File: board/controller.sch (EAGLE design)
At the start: 70 parts, among them J1 X, J10 FEED_HOLD, J11 PROBE, J12 ERROR, J13 HOLDING, J14 GND, J15 MOTOR_CURRENT, J16 SD_READER, J17 WHEEL, J19 Z_DISPLAY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

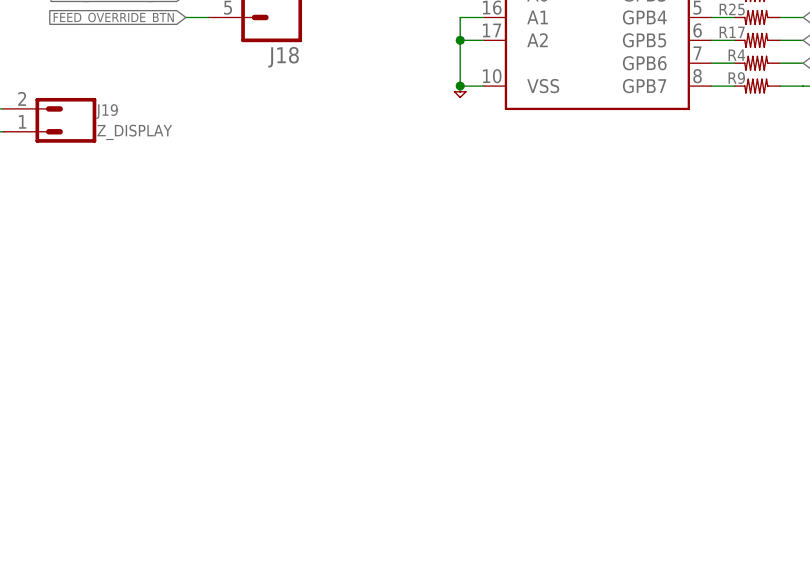
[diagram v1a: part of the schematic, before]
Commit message: updated wemos silk, added info to notes
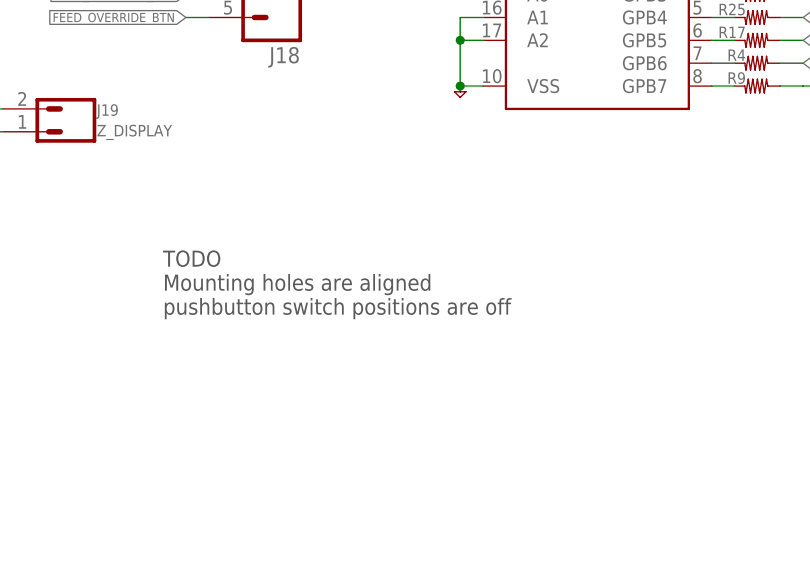
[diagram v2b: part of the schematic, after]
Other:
- note added: "TODO Mounting holes are aligned pushbutton switch positions are off"
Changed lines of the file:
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@@
 <text x="177.8" y="10.16" size="2.54" layer="97" align="top-left">180804</text>
 <text x="261.62" y="10.16" size="2.54" layer="97" align="top-left">v1.0</text>
+<text x="134.62" y="81.28" size="1.778" layer="97">TODO
+Mounting holes are aligned
+pushbutton switch positions are off</text>
 </plain>
 <instances>

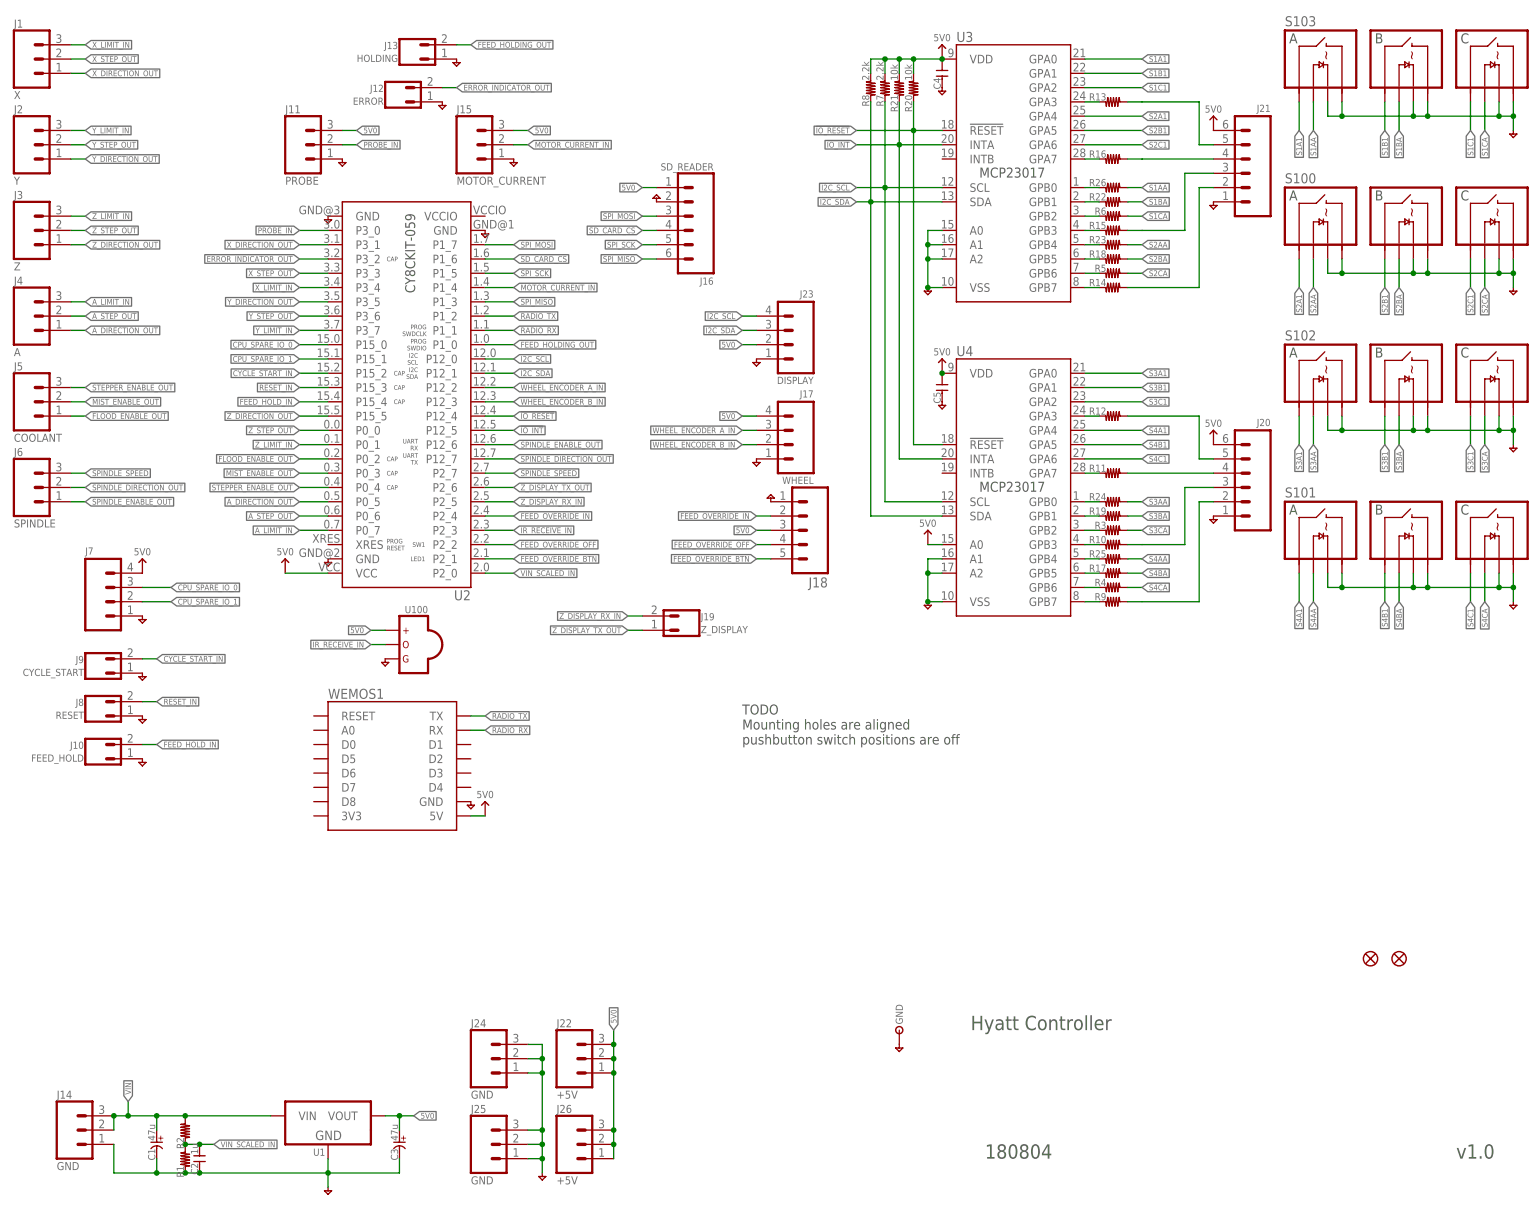
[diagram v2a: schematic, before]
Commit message: added component values to schematic cleaned up brd layout
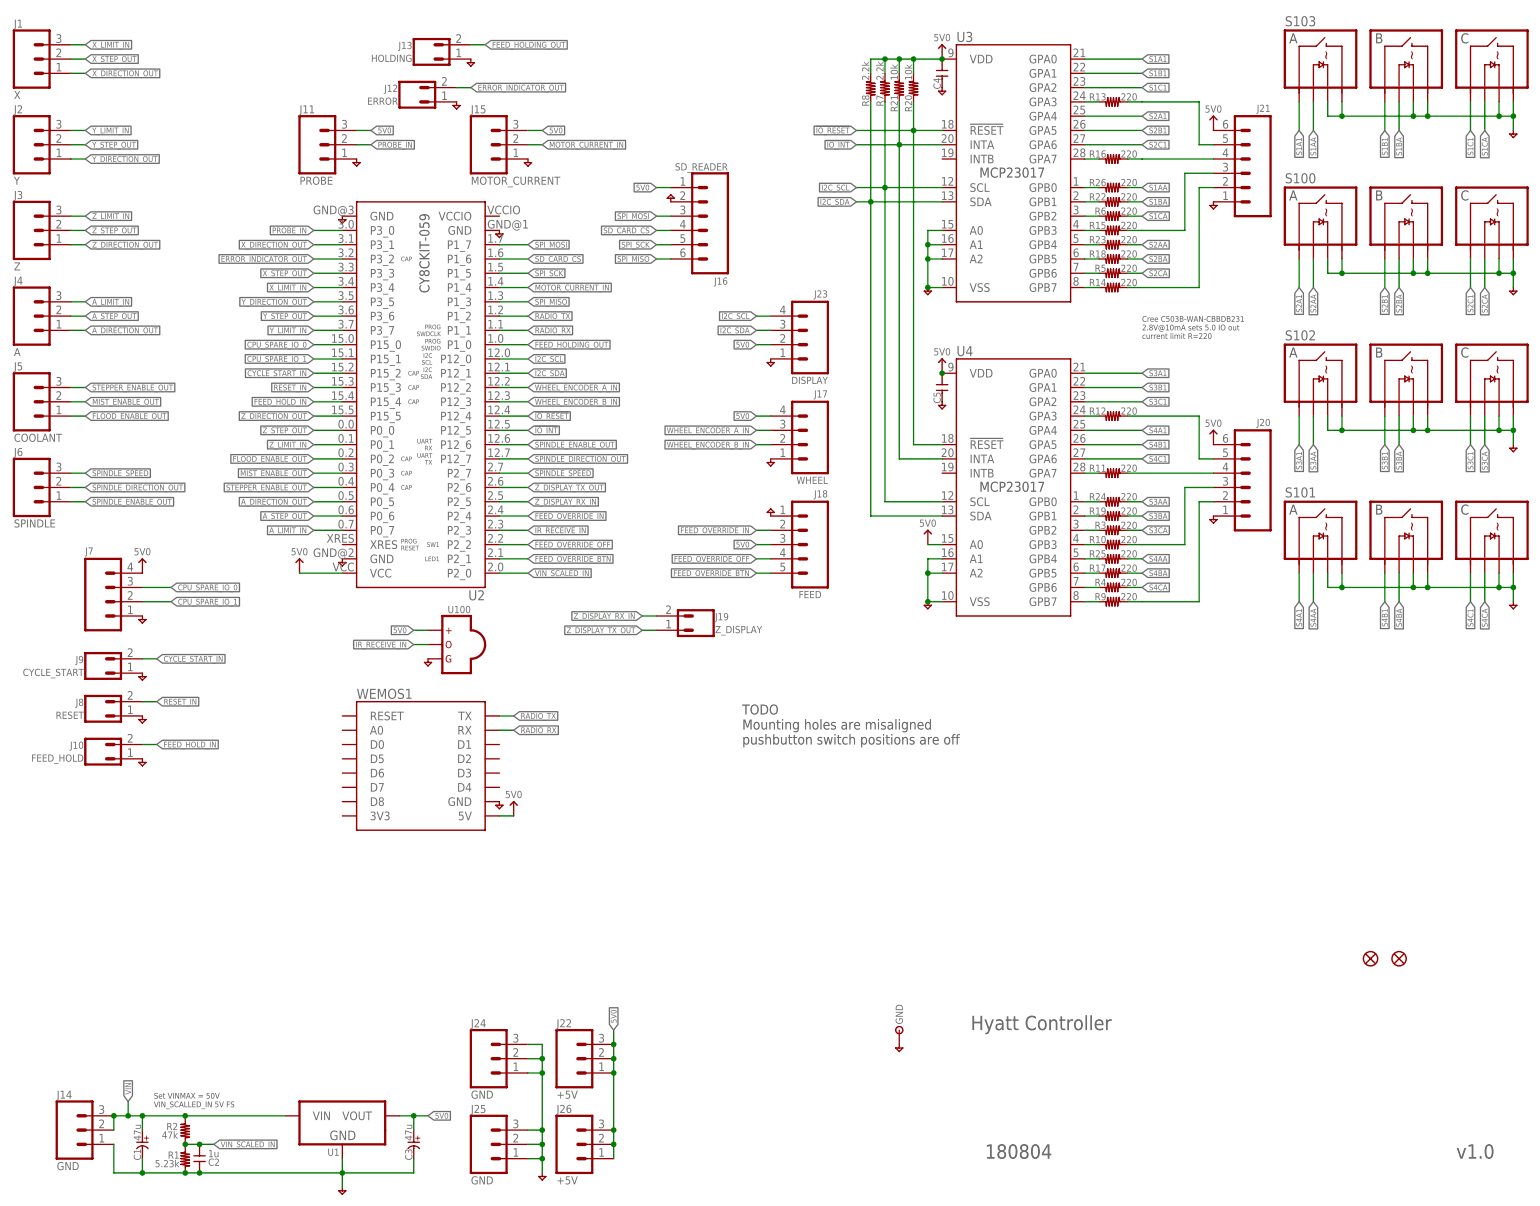
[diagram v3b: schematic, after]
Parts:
- J18: value (none) -> FEED
- R1: value (none) -> 5.23k
- R10, R11, R12, R13, R14, R15, R16, R17, R18, R19, R22, R23, R24, R25, R26, R3, R4, R5, R6, R9: value (none) -> 220
- R2: value (none) -> 47k
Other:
- note added: "Cree C503B-WAN-CBBDB231 2.8V@10mA sets 5.0 IO out current limit R=220"
- note added: "Set VINMAX = 50V VIN_SCALLED_IN 5V FS"
- note added: "TODO Mounting holes are misaligned pushbutton switch positions are off"
- note removed: "TODO Mounting holes are aligned pushbutton switch positions are off"
- moved on the sheet: C1, C3, J11, J12, J13, J15, J16, J17, J18, J19, J23, U1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

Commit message: updated schematic info initial add for rest
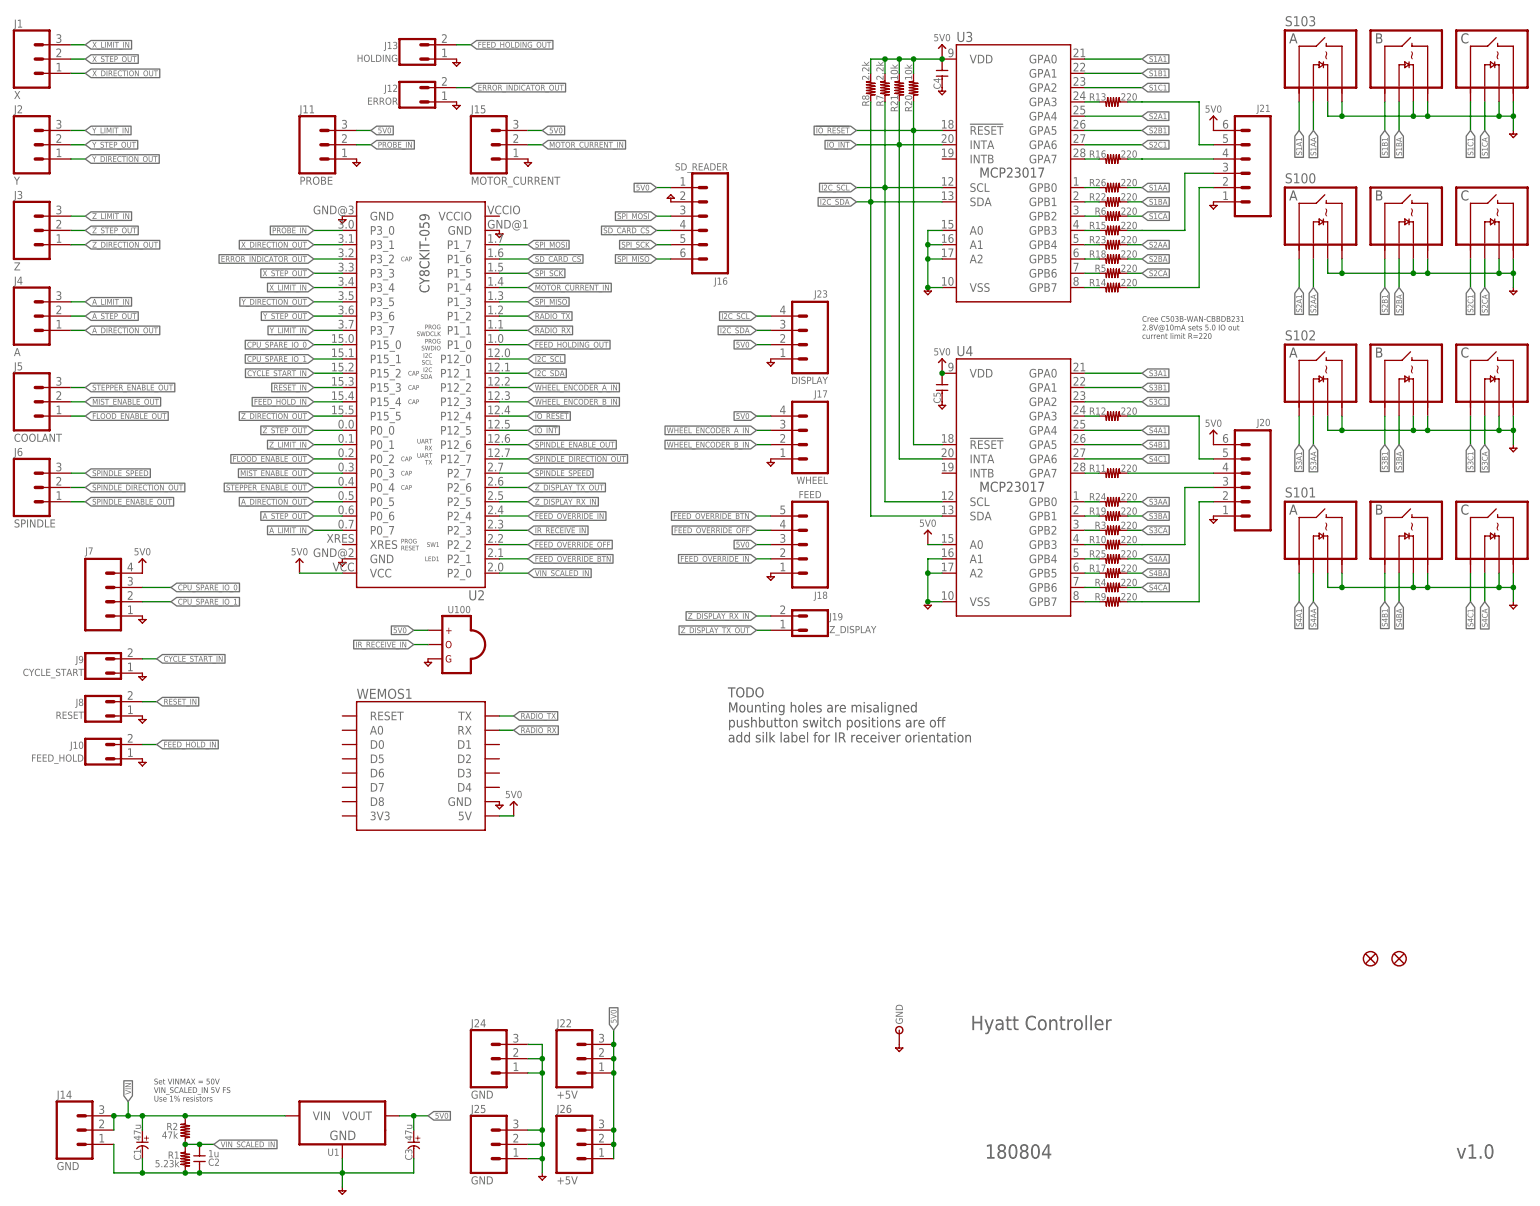
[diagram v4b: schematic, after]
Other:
- note added: "Set VINMAX = 50V VIN_SCALED_IN 5V FS Use 1% resistors"
- note added: "TODO Mounting holes are misaligned pushbutton switch positions are off add silk label for IR receiver orientation"
- note removed: "Set VINMAX = 50V VIN_SCALLED_IN 5V FS"
- note removed: "TODO Mounting holes are misaligned pushbutton switch positions are off"
- moved on the sheet: J13, J18, J19
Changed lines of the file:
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@@
 <text x="177.8" y="10.16" size="2.54" layer="97" align="top-left">180804</text>
 <text x="261.62" y="10.16" size="2.54" layer="97" align="top-left">v1.0</text>
-<text x="134.62" y="81.28" size="1.778" layer="97">TODO
+<text x="132.08" y="91.44" size="1.778" layer="97" align="top-left">TODO
 Mounting holes are misaligned
-pushbutton switch positions are off</text>
+pushbutton switch positions are off
+add silk label for IR receiver orientation</text>
 <text x="205.74" y="157.48" size="1.016" layer="97" align="top-left">Cree C503B-WAN-CBBDB231
 2.8V@10mA sets 5.0 IO out
 current limit R=220</text>
-<text x="29.972" y="19.304" size="1.016" layer="97" align="top-left">Set VINMAX = 50V
-VIN_SCALLED_IN 5V FS</text>
+<text x="29.972" y="21.844" size="1.016" layer="97" align="top-left">Set VINMAX = 50V
+VIN_SCALED_IN 5V FS
+Use 1% resistors</text>
 </plain>
 <instances>
@@
 <instance part="WEMOS1" gate="D1" x="76.2" y="76.2"/>
 <instance part="J8" gate="G$1" x="22.86" y="86.36"/>
-<instance part="J19" gate="G$1" x="124.46" y="101.6" rot="MR0"/>
+<instance part="J19" gate="G$1" x="144.78" y="101.6" rot="MR0"/>
 <instance part="J10" gate="G$1" x="22.86" y="78.74"/>
 <instance part="J9" gate="G$1" x="22.86" y="93.98"/>
@@
 <instance part="J11" gate="G$1" x="60.96" y="187.96"/>
 <instance part="GND12" gate="1" x="66.04" y="185.42"/>
-<instance part="GND13" gate="1" x="139.7" y="121.92" rot="R180"/>
+<instance part="GND13" gate="1" x="139.7" y="111.76" rot="MR0"/>
 <instance part="J15" gate="G$1" x="91.44" y="187.96"/>
 <instance part="GND14" gate="1" x="96.52" y="185.42"/>
@@
 <instance part="GND17" gate="1" x="139.7" y="149.86" rot="MR0"/>
 <instance part="J12" gate="G$1" x="78.74" y="195.58"/>
-<instance part="J13" gate="G$1" x="81.28" y="203.2"/>
+<instance part="J13" gate="G$1" x="78.74" y="203.2"/>
 <instance part="GND18" gate="1" x="83.82" y="195.58"/>
-<instance part="GND19" gate="1" x="86.36" y="203.2"/>
+<instance part="GND19" gate="1" x="83.82" y="203.2"/>
 <instance part="J16" gate="G$1" x="127" y="170.18" rot="R180"/>
 <instance part="GND22" gate="1" x="121.92" y="177.8" rot="R180"/>
@@
 <instance part="GND34" gate="1" x="91.44" y="71.12"/>
 <instance part="P+7" gate="G$1" x="93.98" y="71.12"/>
-<instance part="J18" gate="G$1" x="147.32" y="116.84" smashed="yes" rot="R180">
-<attribute name="NAME" x="149.86" y="126.492" size="1.27" layer="95" rot="R180"/>
-<attribute name="VALUE" x="144.653" y="107.315" size="1.27" layer="96"/>
+<instance part="J18" gate="G$1" x="147.32" y="116.84" smashed="yes" rot="MR0">
+<attribute name="NAME" x="149.86" y="107.188" size="1.27" layer="95" rot="MR0"/>
+<attribute name="VALUE" x="144.653" y="126.365" size="1.27" layer="96" rot="MR180"/>
 </instance>
 <instance part="R2" gate="G$1" x="35.56" y="12.7" smashed="yes" rot="R90">
@@
 <segment>
 <wire x1="139.7" y1="116.84" x2="137.16" y2="116.84" width="0.1524" layer="91"/>
-<label x="137.16" y="116.84" size="1.016" layer="95" rot="R180" xref="yes"/>
+<label x="137.16" y="116.84" size="1.016" layer="95" rot="MR0" xref="yes"/>
 <pinref part="J18" gate="G$1" pin="3"/>
 </segment>
@@
 <net name="FEED_OVERRIDE_IN" class="0">
 <segment>
-<wire x1="139.7" y1="119.38" x2="137.16" y2="119.38" width="0.1524" layer="91"/>
-<label x="137.16" y="119.38" size="1.016" layer="95" rot="R180" xref="yes"/>
+<wire x1="139.7" y1="114.3" x2="137.16" y2="114.3" width="0.1524" layer="91"/>
+<label x="137.16" y="114.3" size="1.016" layer="95" rot="MR0" xref="yes"/>
 <pinref part="J18" gate="G$1" pin="2"/>
 </segment>
@@
 <segment>
 <pinref part="J13" gate="G$1" pin="2"/>
-<wire x1="86.36" y1="205.74" x2="88.9" y2="205.74" width="0.1524" layer="91"/>
-<label x="88.9" y="205.74" size="1.016" layer="95" xref="yes"/>
+<wire x1="83.82" y1="205.74" x2="86.36" y2="205.74" width="0.1524" layer="91"/>
+<label x="86.36" y="205.74" size="1.016" layer="95" xref="yes"/>
 </segment>
 <segment>
@@
 <segment>
 <pinref part="J19" gate="G$1" pin="2"/>
-<wire x1="119.38" y1="104.14" x2="116.84" y2="104.14" width="0.1524" layer="91"/>
-<label x="116.84" y="104.14" size="1.016" layer="95" rot="MR0" xref="yes"/>
+<wire x1="139.7" y1="104.14" x2="137.16" y2="104.14" width="0.1524" layer="91"/>
+<label x="137.16" y="104.14" size="1.016" layer="95" rot="MR0" xref="yes"/>
 </segment>
 <segment>
@@
 <segment>
 <pinref part="J19" gate="G$1" pin="1"/>
-<wire x1="119.38" y1="101.6" x2="116.84" y2="101.6" width="0.1524" layer="91"/>
-<label x="116.84" y="101.6" size="1.016" layer="95" rot="MR0" xref="yes"/>
+<wire x1="139.7" y1="101.6" x2="137.16" y2="101.6" width="0.1524" layer="91"/>
+<label x="137.16" y="101.6" size="1.016" layer="95" rot="MR0" xref="yes"/>
 </segment>
 <segment>
@@
 <segment>
 <pinref part="J18" gate="G$1" pin="4"/>
-<wire x1="139.7" y1="114.3" x2="137.16" y2="114.3" width="0.1524" layer="91"/>
-<label x="137.16" y="114.3" size="1.016" layer="95" rot="MR0" xref="yes"/>
+<wire x1="139.7" y1="119.38" x2="137.16" y2="119.38" width="0.1524" layer="91"/>
+<label x="137.16" y="119.38" size="1.016" layer="95" rot="R180" xref="yes"/>
 </segment>
 <segment>
@@
 <segment>
 <pinref part="J18" gate="G$1" pin="5"/>
-<wire x1="139.7" y1="111.76" x2="137.16" y2="111.76" width="0.1524" layer="91"/>
-<label x="137.16" y="111.76" size="1.016" layer="95" rot="MR0" xref="yes"/>
-</segment>
-<segment>
+<wire x1="139.7" y1="121.92" x2="137.16" y2="121.92" width="0.1524" layer="91"/>
+<label x="137.16" y="121.92" size="1.016" layer="95" rot="R180" xref="yes"/>
+</segment>
+<segment>

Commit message: updated sch info added pushbutton datasheet
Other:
- note added: "TODO Mounting holes are misaligned pushbutton switch positions are off add silk label for IR receiver orientation fix J16 board label, its hidden with AMP connector FUTURE Change keypad back lighting to WS2818/APF3236SEEZGKQBKC?"
- note removed: "TODO Mounting holes are misaligned pushbutton switch positions are off add silk label for IR receiver orientation"
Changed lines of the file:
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@@
 <setting verticaltext="up"/>
 </settings>
-<grid distance="0.1" unitdist="inch" unit="inch" style="lines" multiple="1" display="no" altdistance="0.01" altunitdist="inch" altunit="inch"/>
+<grid distance="0.1" unitdist="inch" unit="inch" style="lines" multiple="1" display="yes" altdistance="0.01" altunitdist="inch" altunit="inch"/>
 <layers>
 <layer number="1" name="Top" color="4" fill="1" visible="no" active="no"/>
@@
 Mounting holes are misaligned
 pushbutton switch positions are off
-add silk label for IR receiver orientation</text>
+add silk label for IR receiver orientation
+fix J16 board label, its hidden with AMP connector
+FUTURE
+Change keypad back lighting to WS2818/APF3236SEEZGKQBKC?</text>
 <text x="205.74" y="157.48" size="1.016" layer="97" align="top-left">Cree C503B-WAN-CBBDB231
 2.8V@10mA sets 5.0 IO out
